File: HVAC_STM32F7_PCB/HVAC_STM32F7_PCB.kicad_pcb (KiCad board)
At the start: 4 copper layers, 91 parts, among them J1 DC_Jack_5.5x2.1mm, J10 OUT_Signal_connector, J11 OUT_Signal_connector, J12 OUT_Signal_connector, J13 OUT_Signal_connector, J14 Signal_connector, J15 Signal_connector, J16 Signal_connector, J17 Signal_connector, J2 Signal_connector, J3 Signal_connector, J4 Signal_connector, J5 Signal_connector, J6 OUT_Signal_connector, J7 OUT_Signal_connector, J8 OUT_Signal_connector, J9 OUT_Signal_connector, Q1 IRLML9301, U1 LM2596S-5, U2 LM2596S-3.3, U5 TLV9304xPW, U6 TLV9304xPW, U7 ADS8688

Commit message: ADD: PCB design started, power supply, buck converters and input ADC placed
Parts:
- added A1: STM32F746NG DISCO, własne:STM32F7_DISCO, F.Cu at (146.2, 83.5)
- added D4: SOD322, Diode_SMD:D_SOD-323F, F.Cu at (52.8, 31.9)
- added D5: LED, LED_THT:LED_D5.0mm_Clear, F.Cu at (82.3, 23.4)
- added D6: LED, LED_THT:LED_D5.0mm_Clear, F.Cu at (155.5, 31.0)
- added D7: LED, LED_THT:LED_D5.0mm_Clear, F.Cu at (100.5, 44.6)
- added SW1: SLW-1276864-4A-D, slide_switches:SLW-1276864-4A-D_FOOTPRINT, F.Cu at (65.0, 23.4)
- added U3: DAC7568IAPW, własne:dac, F.Cu at (185.4, 61.2)
- moved J13 195.6 mm to (273.5, 153.0)
- moved J12 194.9 mm to (273.5, 140.5)
- moved J11 194.3 mm to (273.5, 128.0)
- moved J10 193.7 mm to (273.5, 115.5)
- moved J9 193.1 mm to (273.5, 103.0)
- moved J8 192.6 mm to (273.5, 90.5)
- moved J7 192.2 mm to (273.5, 78.0)
- moved J6 191.8 mm to (273.5, 65.5)
- moved U6 134.7 mm to (230.8, 123.0)
- moved R12 132.7 mm to (202.8, 124.0)
- moved RF7 132.7 mm to (207.5, 127.0)
- moved RG7 132.7 mm to (212.2, 129.9)
- moved J1 128.2 mm to (29.5, 25.5)
- moved RG8 125.5 mm to (191.5, 143.7)
- moved R13 125.5 mm to (182.0, 137.8)
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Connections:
- C11 pad 1: Net-(J14-SHIELD) -> GNDA
- J14 pad 1: Net-(J14-SHIELD) -> GNDA
- J15 pad 1: Net-(J14-SHIELD) -> GNDA
- J16 pad 1: Net-(J14-SHIELD) -> GNDA
- J17 pad 1: Net-(J14-SHIELD) -> GNDA
- J2 pad 1: Net-(J14-SHIELD) -> GNDA
- J3 pad 1: Net-(J14-SHIELD) -> GNDA
- J4 pad 1: Net-(J14-SHIELD) -> GNDA
- J5 pad 1: Net-(J14-SHIELD) -> GNDA
- R14 pad 1: Net-(C16-Pad1) -> Net-(SW1-B)
- R2 pad 1: Net-(J14-SHIELD) -> GNDA
- U7 pad 1: GND -> Net-(A1-D9)
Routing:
- net Net-(SW1-B): track 0.00 -> 40.8 mm, vias 0 -> 1
- net Net-(D3-A2): track 0.00 -> 32.3 mm, vias 0 -> 1
- net Net-(C16-Pad1): track 0.00 -> 20.8 mm, vias 0 -> 2
- net Net-(D4-A): track 0.00 -> 12.7 mm
- net Net-(F1-Pad1): track 0.00 -> 10.3 mm
- net Net-(Q1-D): track 0.00 -> 9.54 mm, vias 0 -> 2
- net Net-(D5-A): track 0.00 -> 4.00 mm
- added copper zone on F.Cu, net GND
- added copper zone on B.Cu, net GNDA

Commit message: add power and input signal trace
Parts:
- moved J10 87.4 mm to (190.0, 89.8)
- moved J11 87.4 mm to (190.0, 102.2)
- moved J12 87.4 mm to (190.0, 114.8)
- moved J13 87.4 mm to (190.0, 127.2)
- moved J6 87.4 mm to (190.0, 39.8)
- moved J7 87.4 mm to (190.0, 52.2)
- moved J8 87.4 mm to (190.0, 64.8)
- moved J9 87.4 mm to (190.0, 77.2)
- moved U6 56.9 mm to (174.8, 113.0), turned to 90 degrees
- moved RG7 41.5 mm to (180.8, 103.0), turned to -90 degrees
- moved C24 41.2 mm to (178.5, 103.0), turned to 90 degrees
- moved U5 35.4 mm to (167.8, 68.0)
- moved RF7 34.3 mm to (183.0, 103.0), turned to -90 degrees
- moved R12 33.8 mm to (176.2, 103.0), turned to -90 degrees
- moved C21 32.0 mm to (177.0, 76.0)
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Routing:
- net +24V: track 0.00 -> 257.7 mm, vias 0 -> 4
- net +3.3V: track 0.00 -> 191.3 mm, vias 0 -> 3
- net +5V: track 0.00 -> 135.3 mm, vias 0 -> 4
- net GNDA: track 0.00 -> 109.9 mm
- net Net-(A1-D5): track 0.00 -> 82.2 mm, vias 0 -> 2
- net Net-(A1-D8): track 0.00 -> 72.2 mm, vias 0 -> 2
- net Net-(A1-D10): track 0.00 -> 69.2 mm, vias 0 -> 2
- net Net-(J15-SIG): track 0.00 -> 68.9 mm, vias 0 -> 2
- net Net-(J2-SIG): track 0.00 -> 66.3 mm, vias 0 -> 3
- net Net-(A1-D9): track 0.00 -> 65.2 mm, vias 0 -> 2
- net Net-(J3-SIG): track 0.00 -> 57.8 mm, vias 0 -> 2
- net Net-(J17-SIG): track 0.00 -> 54.0 mm, vias 0 -> 2
- net Net-(J16-SIG): track 0.00 -> 41.3 mm, vias 0 -> 2
- net Net-(J4-SIG): track 0.00 -> 36.2 mm, vias 0 -> 3
- net Net-(J14-SIG): track 0.00 -> 35.1 mm, vias 0 -> 3
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
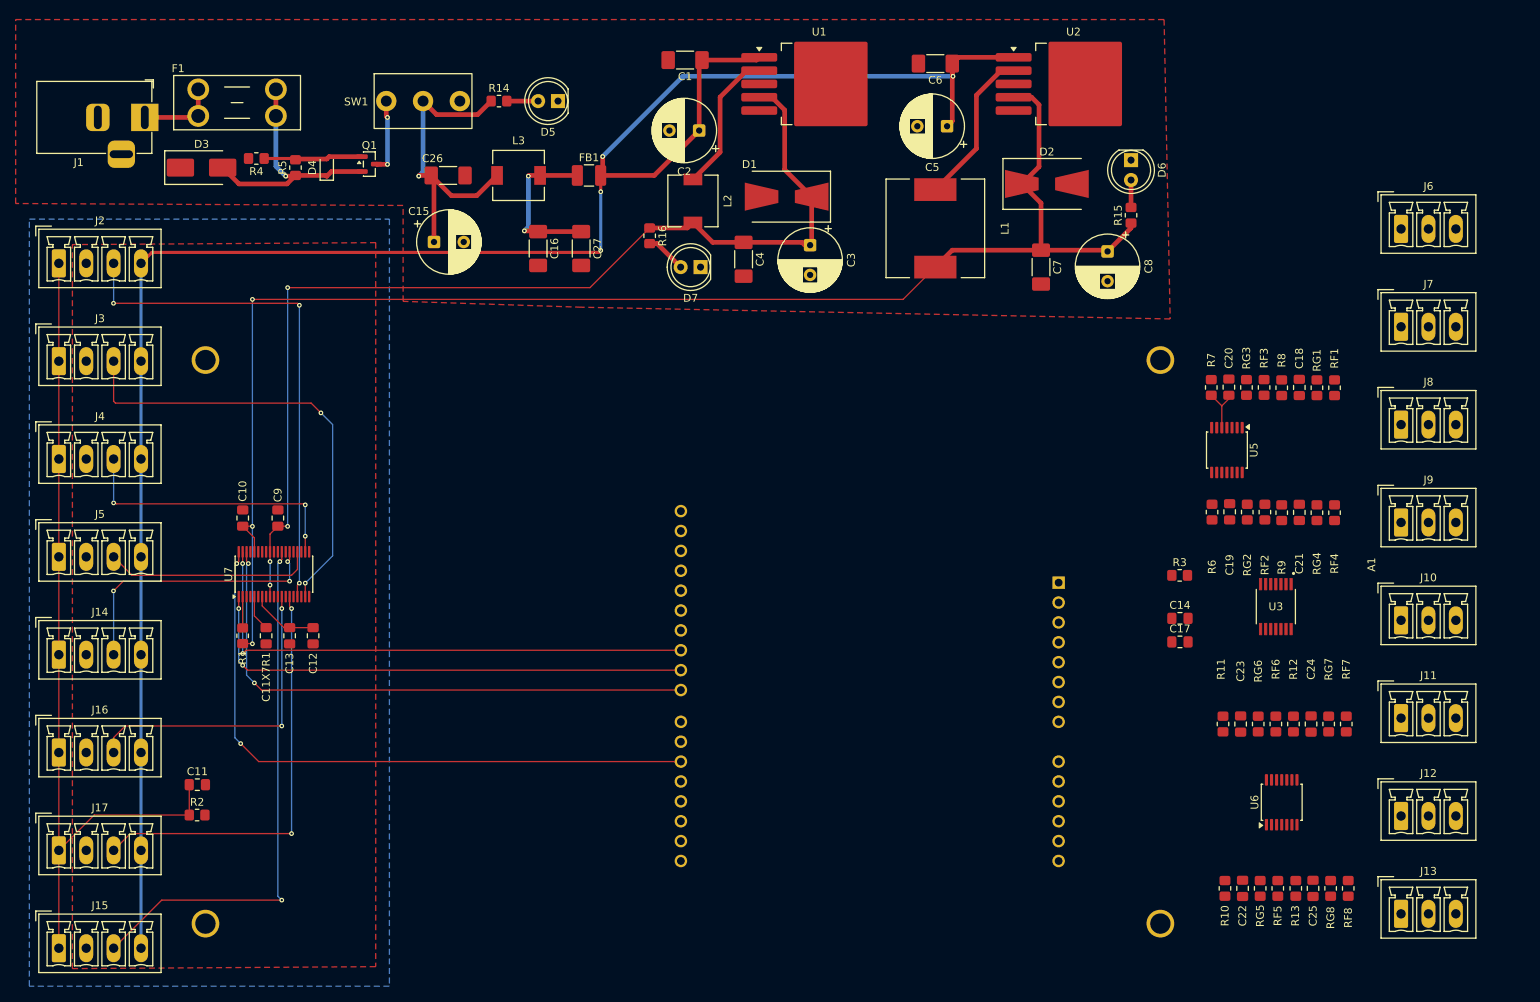
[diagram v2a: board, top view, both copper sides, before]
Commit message: ADD finished pcb traces
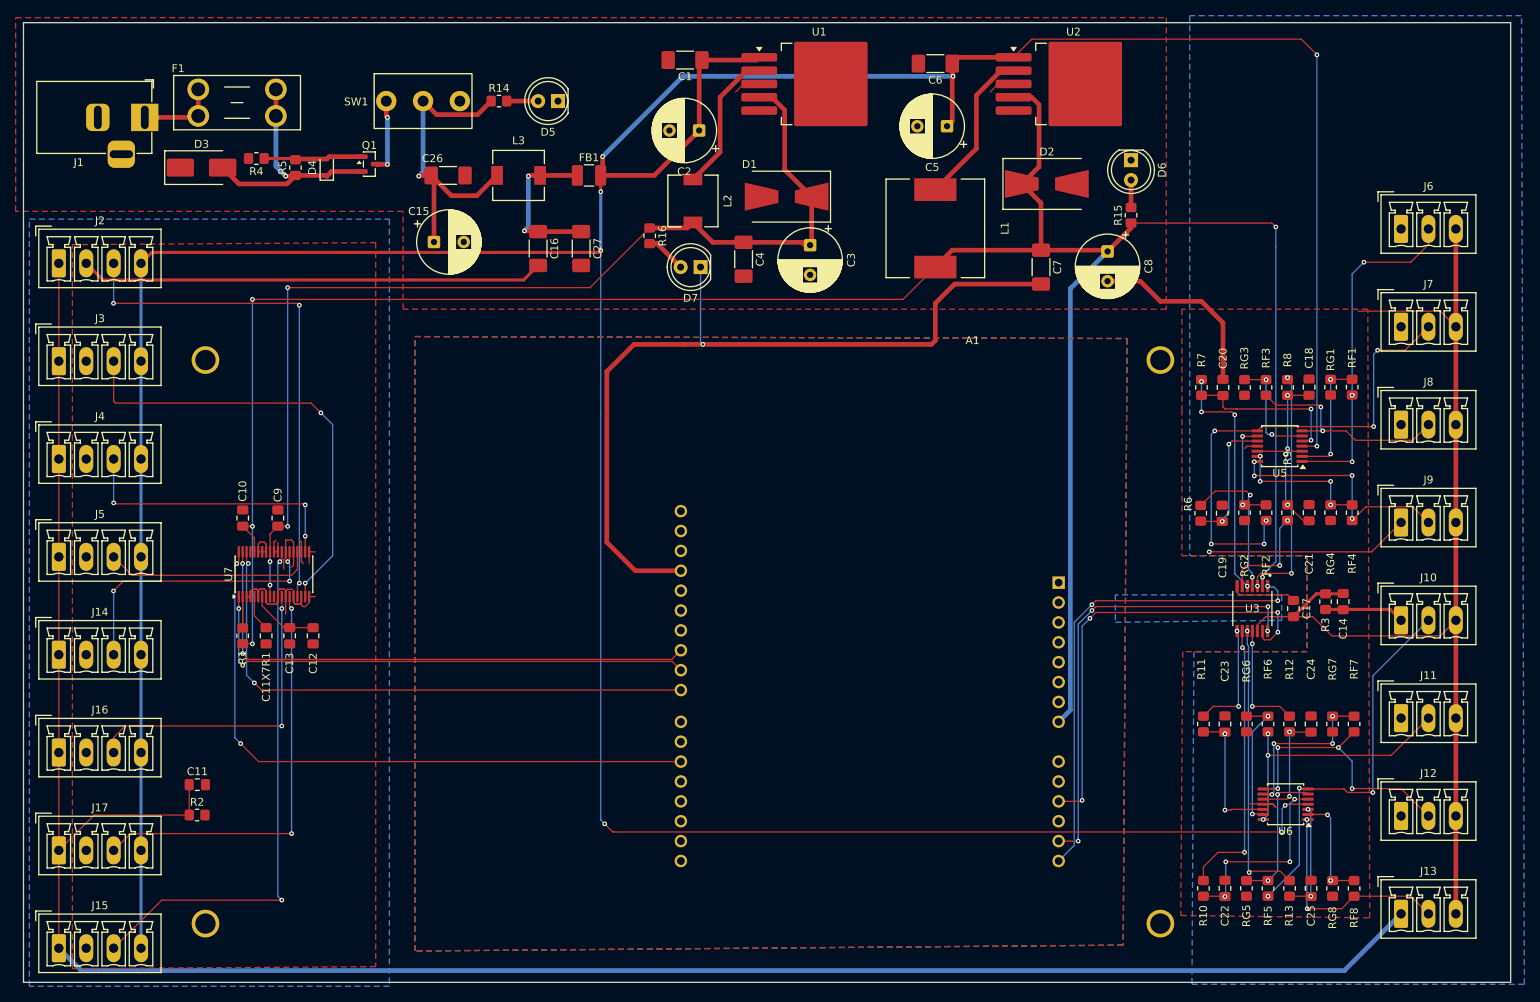
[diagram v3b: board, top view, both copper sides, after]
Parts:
- moved C14 21.0 mm to (182.6, 87.4), turned to 90 degrees
- moved R3 18.9 mm to (180.3, 87.4), turned to 90 degrees
- moved C17 15.1 mm to (176.2, 88.2), turned to -90 degrees
- moved U5 6.77 mm to (174.5, 67.5), turned to 180 degrees
- moved U3 3.01 mm to (171.0, 88.2)
- moved R10 2.75 mm to (164.8, 124.0)
- moved R11 2.50 mm to (164.8, 103.0)
- moved RF1 2.25 mm to (183.8, 60.0)
- moved C22 2.25 mm to (167.5, 124.0)
- moved RF4 2.25 mm to (183.8, 76.0)
- moved C23 2.00 mm to (167.5, 103.0)
- moved RG1 1.75 mm to (181.0, 60.0)
- moved RG4 1.75 mm to (181.0, 76.0)
- moved RG5 1.75 mm to (170.2, 124.0)
- moved RG6 1.50 mm to (170.2, 103.0)
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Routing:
- net GND: track 0.00 -> 384.8 mm, vias 0 -> 1
- net +24V: track 257.7 -> 517.1 mm, vias 4 -> 9
- net GNDA: track 109.9 -> 322.2 mm, vias 0 -> 1
- net +3.3V: track 191.3 -> 319.3 mm, vias 3 -> 5
- net Net-(J7-GND): track 0.00 -> 62.7 mm, vias 0 -> 6
- net NSS_OUT: track 0.00 -> 61.3 mm, vias 0 -> 3
- net SCK_OUT: track 0.00 -> 58.5 mm, vias 0 -> 4
- net MOSI_OUT: track 0.00 -> 56.9 mm, vias 0 -> 4
- net Net-(J10-GND): track 0.00 -> 50.0 mm, vias 0 -> 3
- net Net-(J6-GND): track 0.00 -> 43.7 mm, vias 0 -> 3
- net Net-(U3-VOUTD): track 0.00 -> 36.7 mm, vias 0 -> 2
- net Net-(U3-VOUTF): track 0.00 -> 36.2 mm, vias 0 -> 2
- net Net-(J12-GND): track 0.00 -> 34.9 mm, vias 0 -> 4
- net Net-(J11-GND): track 0.00 -> 33.9 mm, vias 0 -> 3
- net Net-(U3-VOUTE): track 0.00 -> 31.2 mm, vias 0 -> 4
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- added copper zone on B.Cu, net GND
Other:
- board outline added: 190 x 122.6 mm
